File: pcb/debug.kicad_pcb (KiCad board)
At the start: 2 copper layers, 65 parts, among them J1 09732966801, J2 USB_C_Receptacle_USB2.0, Q1 Q_PNP_BCE, SW1 SW_DIP_x02, SW2 Reset, U1 STLQ020PU33R, U2 FT4222HQ, U3 STM32F103V8Tx, U4 INA381AxDSG, U5 SN74ALVC00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

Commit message: start placing components
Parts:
- J1: value 09732966801 -> Val**; footprint 09031966821:Harting-09031966921-0-0-0 -> 09031966821:09032967825
- moved C28 171.5 mm to (101.0, 129.2), turned to -90 degrees
- moved U6 169.1 mm to (97.8, 118.0)
- moved Q1 167.4 mm to (116.0, 144.0)
- moved R1 164.3 mm to (107.0, 126.0), turned to 180 degrees
- moved C2 162.5 mm to (115.0, 136.0)
- moved D1 161.7 mm to (111.0, 144.0), turned to 90 degrees
- moved R2 160.4 mm to (112.0, 140.0)
- moved C1 158.6 mm to (110.0, 135.0), turned to 180 degrees
- moved R17 156.6 mm to (122.2, 140.0)
- moved FB1 155.9 mm to (115.0, 132.0), turned to 90 degrees
- moved R16 155.3 mm to (108.0, 144.0), turned to 90 degrees
- moved JP1 153.4 mm to (116.0, 139.0), turned to 180 degrees
- moved R15 150.9 mm to (112.0, 129.0), turned to 90 degrees
- moved U4 149.2 mm to (107.0, 130.0)
- moved D2 147.3 mm to (121.0, 144.0), turned to 90 degrees
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
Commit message: moved components
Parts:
- moved C10 85.2 mm to (108.0, 70.0)
- moved C11 85.2 mm to (111.0, 69.0)
- moved C12 85.2 mm to (106.8, 64.0)
- moved C13 85.2 mm to (122.0, 65.0)
- moved C14 85.2 mm to (104.0, 74.0)
- moved C15 85.2 mm to (100.0, 70.8)
- moved C6 85.2 mm to (119.0, 61.0)
- moved C7 85.2 mm to (119.0, 63.0)
- moved C8 85.2 mm to (111.0, 72.0)
- moved C9 85.2 mm to (113.0, 69.0)
- moved R10 85.2 mm to (104.0, 68.0)
- moved R11 85.2 mm to (100.0, 68.0)
- moved R3 85.2 mm to (103.8, 53.0)
- moved R4 85.2 mm to (99.0, 52.0)
- moved R5 85.2 mm to (118.0, 69.0)
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
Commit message: move components
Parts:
- moved C22 38.9 mm to (95.0, 104.0), turned to 180 degrees
- moved C16 36.7 mm to (95.0, 101.0), turned to 180 degrees
- moved C27 29.8 mm to (109.0, 81.0), turned to 90 degrees
- moved R13 29.2 mm to (111.0, 110.0), turned to -90 degrees
- moved C18 28.7 mm to (114.0, 109.8), turned to -90 degrees
- moved C17 28.3 mm to (102.0, 86.0), turned to 90 degrees
- moved C26 27.5 mm to (126.0, 98.0), turned to 180 degrees
- moved Y2 27.2 mm to (126.0, 94.0), turned to -90 degrees
- moved C24 26.9 mm to (122.0, 86.0), turned to 180 degrees
- moved R2 24.2 mm to (94.0, 123.8), turned to -90 degrees
- moved C20 23.0 mm to (122.0, 102.0), turned to 0 degrees
- moved FB2 23.0 mm to (122.0, 89.0), turned to 0 degrees
- moved R14 22.6 mm to (96.1, 134.8), turned to 90 degrees
- moved C25 21.2 mm to (123.0, 94.0), turned to 90 degrees
- moved C21 20.2 mm to (122.0, 99.0), turned to 0 degrees
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
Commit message: move components
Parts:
- moved R4 63.5 mm to (112.6, 114.0)
- moved R3 62.6 mm to (117.4, 114.1)
- moved SW1 62.0 mm to (114.4, 119.5)
- moved C13 53.8 mm to (104.3, 115.8), turned to 180 degrees
- moved C6 52.9 mm to (108.3, 112.8), turned to -90 degrees
- moved C7 51.4 mm to (106.3, 112.8), turned to -90 degrees
- moved R7 50.1 mm to (104.3, 112.8), turned to 90 degrees
- moved R6 48.8 mm to (102.3, 112.8), turned to 90 degrees
- moved R5 46.4 mm to (100.3, 111.8), turned to 90 degrees
- moved C26 44.6 mm to (107.7, 57.3), turned to -90 degrees
- moved U2 43.6 mm to (105.0, 107.1), turned to 90 degrees
- moved Y2 42.9 mm to (103.7, 57.3), turned to 0 degrees
- moved C20 42.0 mm to (111.7, 61.3), turned to 90 degrees
- moved R8 41.9 mm to (99.3, 108.8), turned to 180 degrees
- moved C18 40.8 mm to (119.5, 69.3), turned to 0 degrees
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
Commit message: finished placing components
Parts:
- added H1: MountingHole, MountingHole:MountingHole_2.7mm_M2.5, F.Cu at (95.0, 52.0)
- added H2: MountingHole, MountingHole:MountingHole_2.7mm_M2.5, F.Cu at (95.0, 146.0)
- added H3: MountingHole, MountingHole:MountingHole_2.7mm_M2.5, F.Cu at (126.0, 146.0)
- added H4: MountingHole, MountingHole:MountingHole_2.7mm_M2.5, F.Cu at (126.0, 52.0)
- J1: value Val** -> 09032967825
- moved SW2 82.8 mm to (127.0, 61.5), turned to -90 degrees
- moved R12 78.3 mm to (123.5, 61.7), turned to -90 degrees
- moved R11 34.7 mm to (100.5, 128.5)
- moved C15 32.9 mm to (105.5, 126.0), turned to -90 degrees
- moved R19 31.8 mm to (126.1, 139.7), turned to 0 degrees
- moved D2 31.3 mm to (126.0, 115.0), turned to 0 degrees
- moved R10 30.7 mm to (102.5, 128.5), turned to -90 degrees
- moved C10 29.3 mm to (115.0, 125.8), turned to 0 degrees
- moved J2 28.7 mm to (127.3, 131.5), turned to 90 degrees
- moved R15 28.3 mm to (121.5, 141.4), turned to 0 degrees
- moved D1 28.2 mm to (126.0, 120.6), turned to 0 degrees
- moved Y1 27.3 mm to (101.3, 125.0), turned to 0 degrees
- moved C8 26.6 mm to (117.0, 121.5), turned to -90 degrees
- moved R9 26.0 mm to (110.0, 126.0), turned to -90 degrees
- moved R14 25.7 mm to (121.5, 138.9), turned to 180 degrees
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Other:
- board outline added: 50 x 100 mm
- copper layers 2 -> 4
- board text added: "UMXdbg cchaine Rev 1.0 2022"

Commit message: route the power supply
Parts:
- added D3: MMBZxx, Package_TO_SOT_SMD:SOT-23, F.Cu at (115.9, 130.2)
- moved C27 53.5 mm to (107.3, 136.7)
- moved R18 6.92 mm to (126.1, 124.8), turned to 0 degrees
- moved R10 3.34 mm to (103.2, 125.2)
- moved R11 3.34 mm to (101.2, 125.2)
- moved C14 3.34 mm to (102.0, 118.7)
- moved Y1 3.34 mm to (102.0, 121.7)
- moved R19 1.51 mm to (126.1, 138.2)
- moved C10 1.01 mm to (115.5, 125.0)
- moved C11 1.01 mm to (114.5, 120.6)
- moved C12 1.01 mm to (108.5, 125.1)
- moved C13 1.01 mm to (109.5, 108.2)
- moved C15 1.01 mm to (106.0, 125.1)
- moved C6 1.01 mm to (105.5, 111.2)
- moved C7 1.01 mm to (107.5, 111.2)
- moved C8 1.01 mm to (117.5, 120.6)
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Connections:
- net /DM renamed /DN
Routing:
- net /DN: track 0.00 -> 23.7 mm
- net /DP: track 0.00 -> 22.2 mm
- net Net-(U5-Pad8): track 0.00 -> 14.2 mm
- net Net-(U5-Pad10): track 0.00 -> 12.2 mm
- net /Power/OVERCURRENT_SENSE: track 0.00 -> 8.68 mm
- net Net-(J2-PadA5): track 0.00 -> 7.30 mm
- net +3V3: track 0.00 -> 6.53 mm, vias 0 -> 4
- net Net-(J2-PadB5): track 0.00 -> 6.47 mm
- net Net-(R14-Pad2): track 0.00 -> 5.83 mm
- net Net-(U5-Pad2): track 0.00 -> 5.03 mm
- net VBUS: track 0.00 -> 4.66 mm, vias 0 -> 6
- net /Power/UNFILTERED_VBUS: track 0.00 -> 4.60 mm
- net GND: track 0.00 -> 4.23 mm, vias 0 -> 2
- net /Power/OVERCURRENT_BASE: track 0.00 -> 3.33 mm
- net CURRENT_SENSE: track 0.00 -> 2.38 mm
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- added copper zone on F.Cu, net +3V3
- added copper zone on In2.Cu, net +3V3
- added copper zone on F.Cu, net +5V
- added copper zone on F.Cu, net +5V_Mod
- added copper zone on In2.Cu, net +5V_Mod
- added copper zone on F.Cu, net /Power/UNFILTERED_VBUS
- added copper zone on In1.Cu, net GND
- added copper zone on B.Cu, net VBUS
- added copper zone on F.Cu, net VBUS

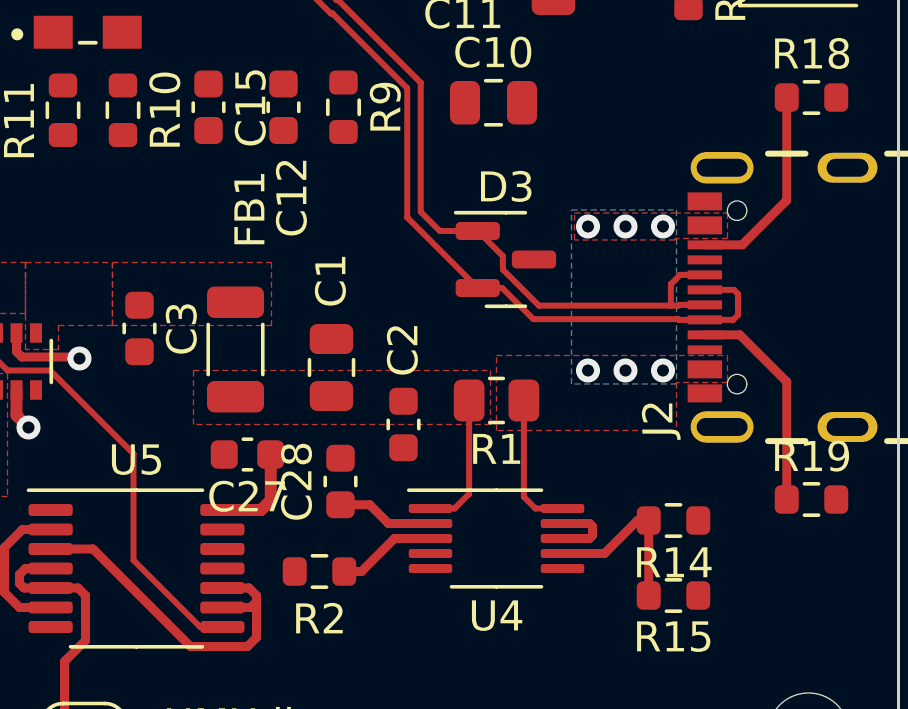
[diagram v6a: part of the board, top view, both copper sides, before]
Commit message: add missing 3d models
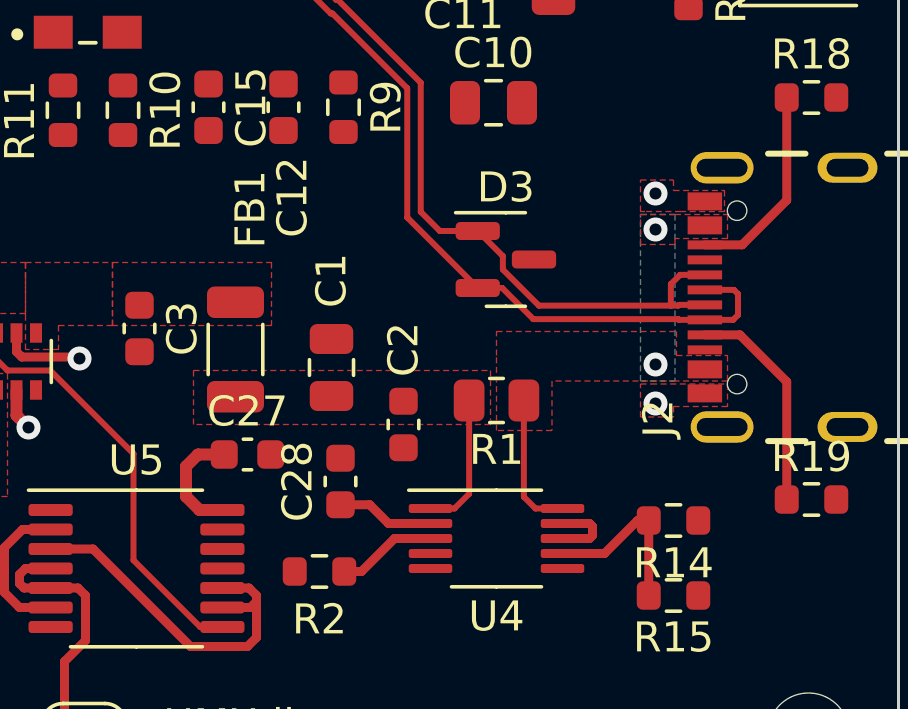
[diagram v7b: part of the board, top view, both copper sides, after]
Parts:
- turned C27 to 0 degrees
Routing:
- net +3V3: track 6.53 -> 7.10 mm
- net VBUS: vias 6 -> 2
- net GND: vias 2 -> 4
- added copper zone on F.Cu, net GND

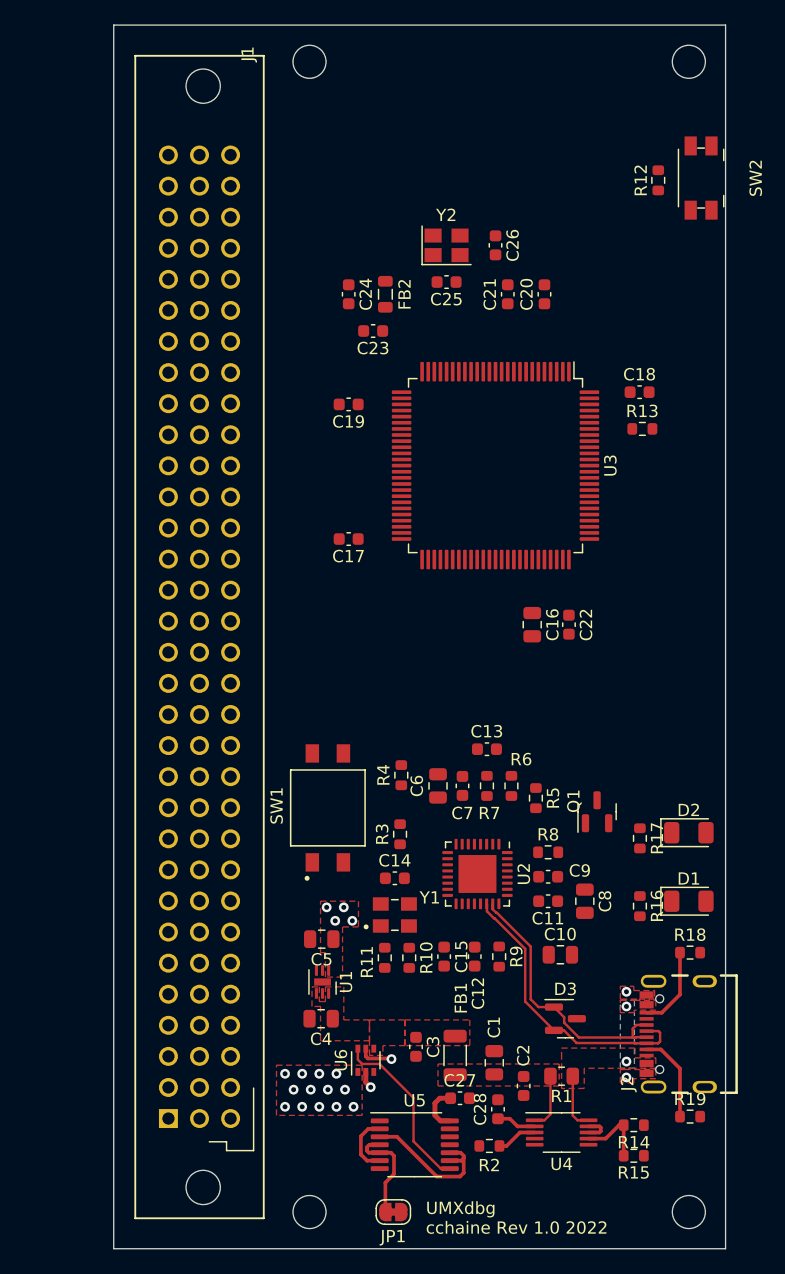
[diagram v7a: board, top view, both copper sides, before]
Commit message: route more components
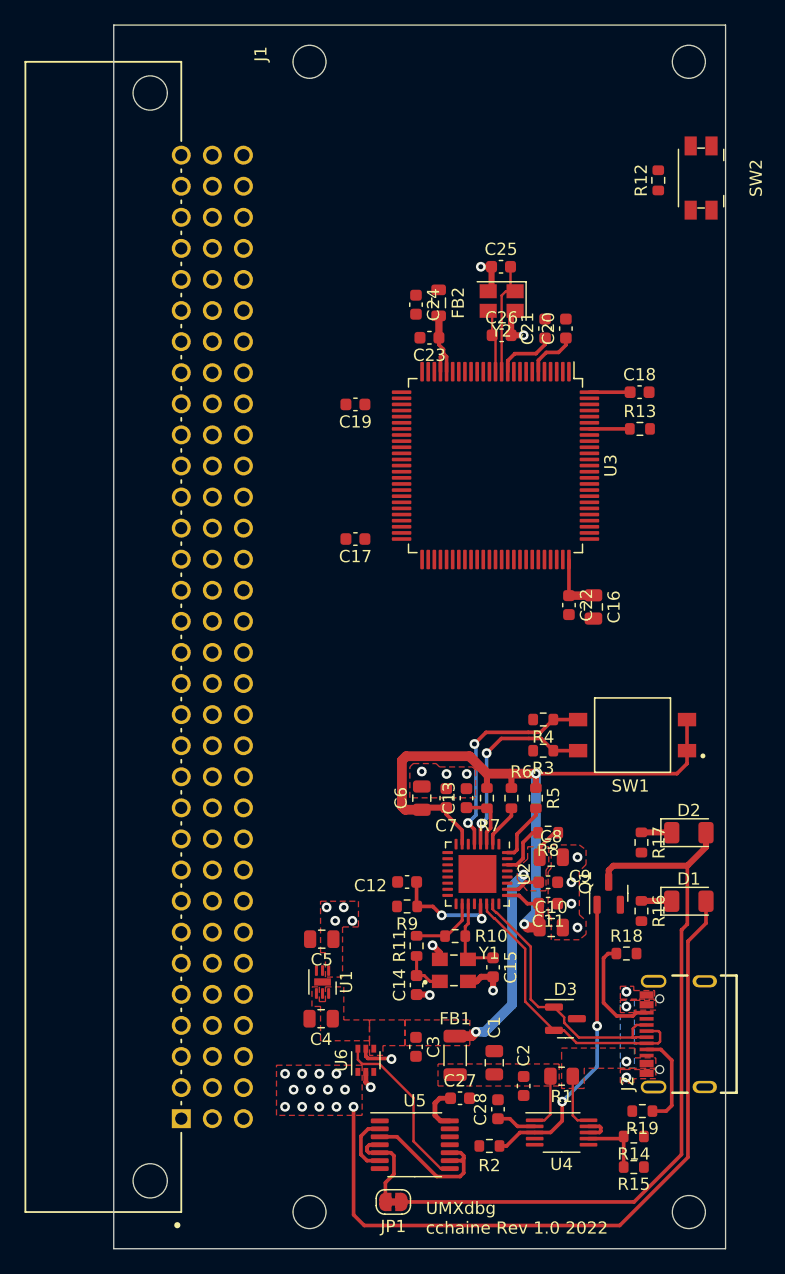
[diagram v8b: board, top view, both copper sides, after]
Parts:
- J1: footprint 09031966821:09032967825 -> 09031966821:Harting-09031966921-0-0-0
- moved SW1 25.6 mm to (121.4, 107.0), turned to 180 degrees
- moved R3 13.5 mm to (114.1, 108.3), turned to 180 degrees
- moved R4 12.5 mm to (114.1, 105.8), turned to 180 degrees
- moved C14 8.90 mm to (103.8, 127.5), turned to -90 degrees
- moved R9 8.57 mm to (103.0, 121.0), turned to 180 degrees
- moved C12 8.23 mm to (103.0, 119.0), turned to 0 degrees
- moved J1 7.80 mm to (78.2, 99.0)
- moved C26 7.37 mm to (110.7, 74.3), turned to 0 degrees
- moved Q1 6.73 mm to (119.5, 120.0)
- moved Y1 6.61 mm to (106.8, 126.2)
- moved Y2 6.40 mm to (110.7, 71.5), turned to 180 degrees
- moved C24 5.57 mm to (103.7, 71.8)
- moved C16 5.21 mm to (118.2, 96.5)
- moved R18 5.20 mm to (120.9, 124.9)
- moved C23 4.63 mm to (104.8, 74.5)
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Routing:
- net /VCCIO: track 0.00 -> 61.6 mm, vias 0 -> 2
- net +5V_Mod: track 0.00 -> 60.4 mm
- net Net-(D2-Pad2): track 0.00 -> 59.2 mm
- net +5V: track 0.00 -> 22.4 mm, vias 0 -> 2
- net /Power/OVERCURRENT_BASE: track 3.33 -> 24.8 mm, vias 0 -> 2
- net /DCNF1: track 0.00 -> 18.0 mm, vias 0 -> 2
- net +3V3: track 7.10 -> 24.7 mm
- net /DCNF0: track 0.00 -> 16.0 mm, vias 0 -> 2
- net GND: track 4.23 -> 18.6 mm, vias 4 -> 16
- net /MCU/OSC_IN: track 0.00 -> 9.63 mm
- net /RREF: track 0.00 -> 8.96 mm, vias 0 -> 2
- net /XSCO: track 0.00 -> 6.84 mm
- net /MCU/VDDA: track 0.00 -> 6.41 mm
- net /XSCI: track 0.00 -> 5.87 mm
- net /MCU/OSC_OUT: track 0.00 -> 5.22 mm
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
